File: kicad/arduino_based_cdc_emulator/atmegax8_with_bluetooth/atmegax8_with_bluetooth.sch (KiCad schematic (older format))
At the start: 66 parts, among them IC1 ATMEGA88-A, P1 CONN_9, P2 SPI, Q1 BC817-40, U1 78L05, U2 S3860M-S, U3 LM358, X1 16MHz

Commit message: PCB layout work
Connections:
- net AOUTR: now also P1.3 (P3); no longer P1.2 (P2)
- net GNDA: now also P1.2 (P2); no longer P1.3 (P3)
- net MIC: no longer C23.2, P1.4 (P4), R27.1
- new net MIC_IN: C23.2, P1.4 (P4), R27.1
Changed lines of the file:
@@
 Text Label 7400 9450 0    60   ~ 0
 AOUTL
-Text Label 7400 9550 0    60   ~ 0
+Text Label 7400 9650 0    60   ~ 0
 AOUTR
 Text Label 7250 10450 0    60   ~ 0
@@
 	7250 10450 7900 10450
 Wire Wire Line
-	7250 9650 7900 9650
-Wire Wire Line
-	7900 9550 7400 9550
+	7900 9650 7400 9650
 Wire Wire Line
 	7900 9450 7400 9450
@@
 	7700 10150 7900 10150
 Wire Wire Line
-	7250 9650 7250 9300
-Wire Wire Line
 	2950 8150 3800 8150
 Text Label 9100 6950 2    60   ~ 0
@@
 $EndComp
 Text Label 10550 5850 2    60   ~ 0
-MIC
+MIC_IN
 Text Label 7400 9750 0    60   ~ 0
-MIC
+MIC_IN
 Wire Wire Line
 	7400 9750 7900 9750
@@
 	7800 9850 7800 10050
 Connection ~ 7800 10050
+Wire Wire Line
+	7250 9300 7250 9550
+Wire Wire Line
+	7250 9550 7900 9550
 $EndSCHEMATC

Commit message: PCB layout work
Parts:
- C24: value 2u1 -> 2u2
- renumbered R4*1 to R4
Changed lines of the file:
@@
 P 6900 8550
 F 0 "C24" H 6950 8650 50  0000 L CNN
-F 1 "2u1" H 6950 8450 50  0000 L CNN
+F 1 "2u2" H 6950 8450 50  0000 L CNN
 F 2 "Capacitors_Tantalum_SMD:TantalC_SizeA_EIA-3216_HandSoldering" H 6900 8550 60  0001 C CNN
 F 3 "" H 6900 8550 60  0001 C CNN
@@
 BT_ENABLE
 $Comp
-L R R4*1
+L R R4
 U 1 1 568C17BF
 P 3350 6350
-F 0 "R4*1" V 3430 6350 50  0000 C CNN
+F 0 "R4" V 3430 6350 50  0000 C CNN
 F 1 "3k3" V 3350 6350 50  0000 C CNN
 F 2 "Resistors_SMD:R_0805_HandSoldering" H 3350 6350 60  0001 C CNN

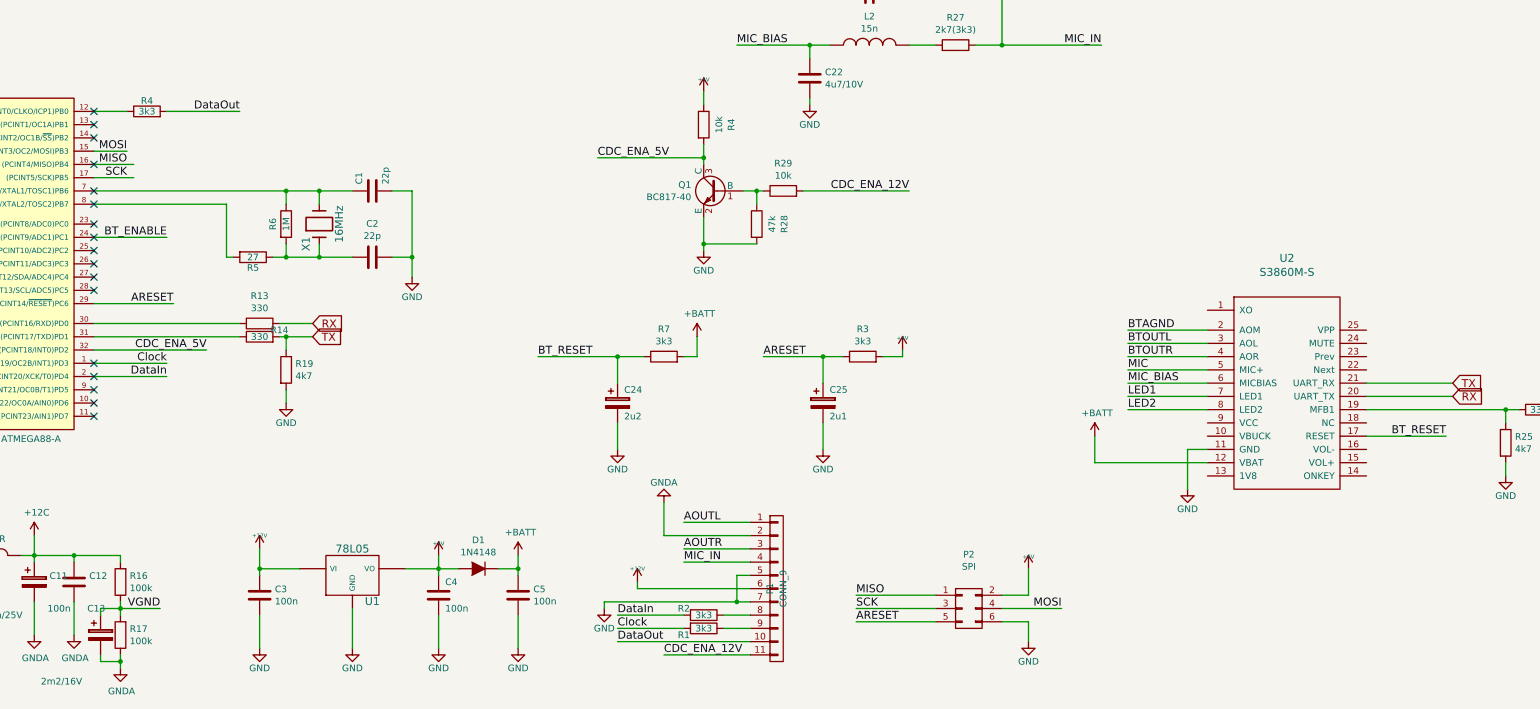
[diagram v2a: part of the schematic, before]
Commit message: finished? I gues yes, board for vwcdavr emulator with bluetooth
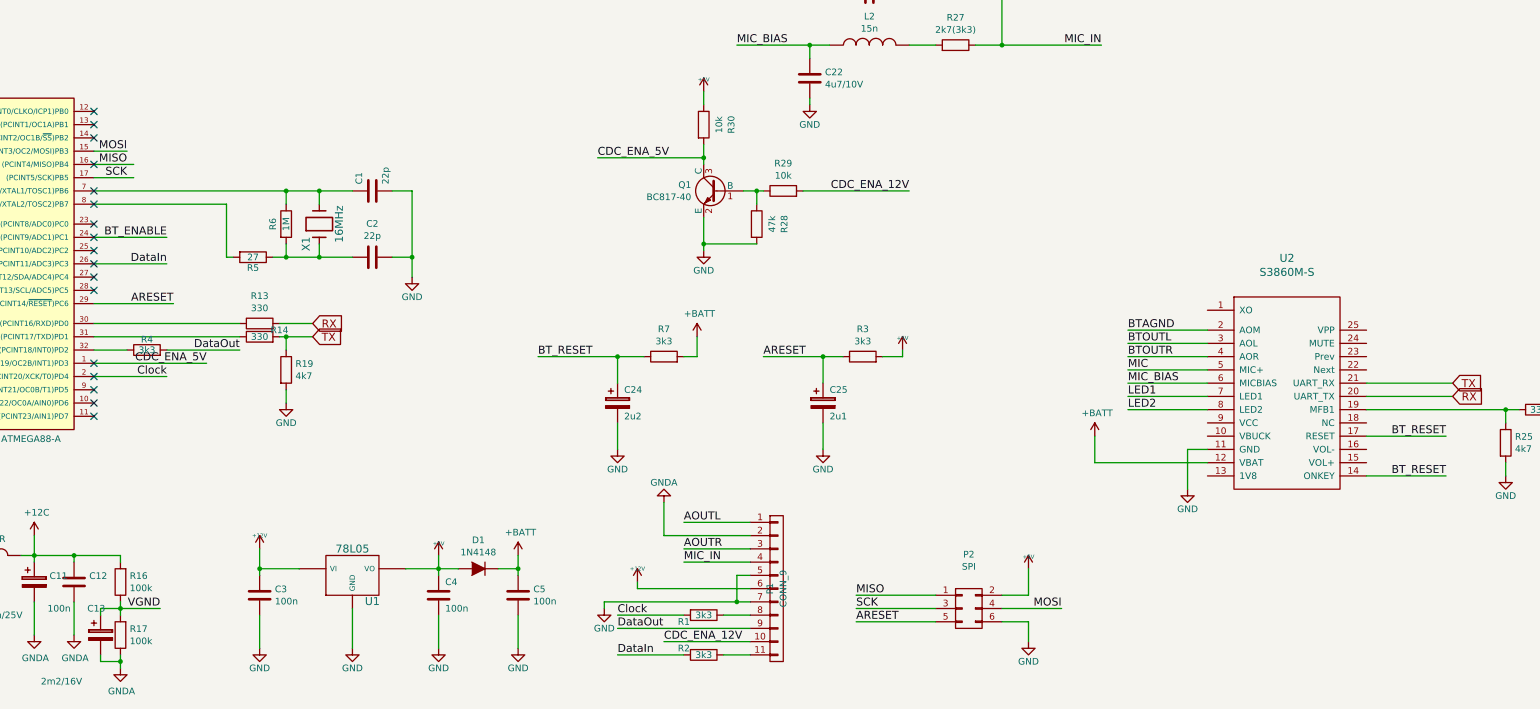
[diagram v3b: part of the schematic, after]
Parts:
- renumbered R4 to R30
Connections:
- net BT_RESET: now also U2.14 (ONKEY)
- net CDC_ENA_12V: now also P1.10 (P10); no longer P1.11 (P11)
- net CDC_ENA_5V: now also IC1.1 ((PCINT19/OC2B/INT1)PD3); no longer IC1.32 ((PCINT18/INT0)PD2)
- net Clock: now also IC1.2 ((PCINT20/XCK/T0)PD4); no longer IC1.1 ((PCINT19/OC2B/INT1)PD3)
- net DataIn: now also IC1.26 ((PCINT11/ADC3)PC3); no longer IC1.2 ((PCINT20/XCK/T0)PD4)
- net DataOut: now also P1.9 (P9); no longer P1.10 (P10)
- net at IC1.12 ((PCINT0/CLKO/ICP1)PB0): no longer R4.1
- net at R1.1: now also P1.8 (P8); no longer P1.9 (P9)
- net at R2.1: now also P1.11 (P11); no longer P1.8 (P8)
- new net: IC1.32 ((PCINT18/INT0)PD2), R4.1
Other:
- moved on the sheet: R1, R2, R4
